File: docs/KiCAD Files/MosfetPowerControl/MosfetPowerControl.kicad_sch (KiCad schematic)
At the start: 9 parts, among them J1 Screw_Terminal_01x03, Q1 FDS6898A, Q2 FDS6898A, Q3 FDS6898A, Q4 FDS6898A

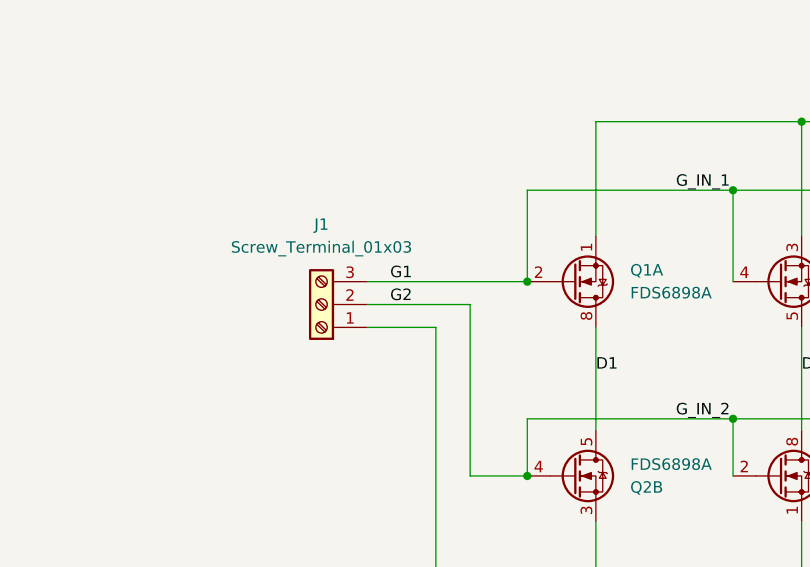
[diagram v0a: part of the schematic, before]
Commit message: changed truth table
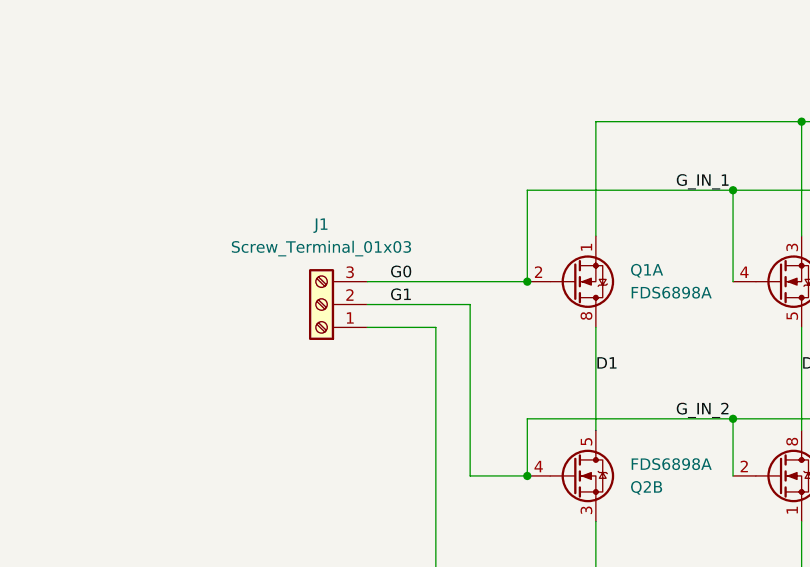
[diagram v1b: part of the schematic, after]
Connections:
- net G1: now also J1.2 (Pin_2), Q2.2 (G1), Q2.4 (G2), Q4.2 (G1), Q4.4 (G2); no longer J1.3 (Pin_3), Q1.2 (G1), Q1.4 (G2), Q3.2 (G1), Q3.4 (G2)
- net G2: no longer J1.2 (Pin_2), Q2.2 (G1), Q2.4 (G2), Q4.2 (G1), Q4.4 (G2)
- new net G0: J1.3 (Pin_3), Q1.2 (G1), Q1.4 (G2), Q3.2 (G1), Q3.4 (G2)
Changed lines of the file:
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@@
     (effects (font (size 1.27 1.27)) (justify left bottom))
   )
-  (label "G2" (at 156.21 101.6 0) (fields_autoplaced)
+  (label "G1" (at 156.21 101.6 0) (fields_autoplaced)
     (effects (font (size 1.27 1.27)) (justify left bottom))
   )
@@
     (effects (font (size 1.27 1.27)) (justify left bottom))
   )
-  (label "G1" (at 156.21 99.06 0) (fields_autoplaced)
+  (label "G0" (at 156.21 99.06 0) (fields_autoplaced)
     (effects (font (size 1.27 1.27)) (justify left bottom))
   )
